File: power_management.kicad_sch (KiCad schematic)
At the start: 18 parts, among them Q1 Q_NMOS_DGS, Q2 Q_NMOS_DGS, U2 TLV803EA24DCKR

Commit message: WIP
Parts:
- added J2 (x3): Conn_01x04_Socket, Connector_PinHeader_2.54mm:PinHeader_1x04_P2.54mm_Vertical, symbol Connector:Conn_01x04_Socket
- R18: renamed from R17; footprint (none) -> Resistor_SMD:R_0603_1608Metric_Pad0.98x0.95mm_HandSolder
- R19: renamed from R18; footprint (none) -> Resistor_SMD:R_0603_1608Metric_Pad0.98x0.95mm_HandSolder
- R20: renamed from R19; footprint (none) -> Resistor_SMD:R_0603_1608Metric_Pad0.98x0.95mm_HandSolder
- R21: renamed from R20; footprint (none) -> Resistor_SMD:R_0603_1608Metric_Pad0.98x0.95mm_HandSolder
- R22: renamed from R21; footprint (none) -> Resistor_SMD:R_0603_1608Metric_Pad0.98x0.95mm_HandSolder
- R23: renamed from R22; footprint (none) -> Resistor_SMD:R_0603_1608Metric_Pad0.98x0.95mm_HandSolder
- R24: renamed from R23; footprint (none) -> Resistor_SMD:R_0603_1608Metric_Pad0.98x0.95mm_HandSolder
- R25: renamed from R24; footprint (none) -> Resistor_SMD:R_0603_1608Metric_Pad0.98x0.95mm_HandSolder
- R? (x2): footprint (none) -> Resistor_SMD:R_0603_1608Metric_Pad0.98x0.95mm_HandSolder
- U? (x2): footprint (none) -> Package_TO_SOT_SMD:SOT-23-6_Handsoldering
- renumbered R16 to R17
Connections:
- net EN_{PULSE}: now also J2.2 (Pin_2)
- net EN_{V_{BOOST3.3}}: now also J2.1 (Pin_1)
- net FORCE_ON: now also J2.2 (Pin_2)
- net GND: now also J2.1 (Pin_1)
- net SHD: now also J2.3 (Pin_3)
- net V_{ADP_SENSE_EN}: now also J2.1 (Pin_1)
- net V_{ADP_SENSE}: now also J2.2 (Pin_2)
- net V_{ADP}: now also J2.4 (Pin_4)
- net V_{RTC_SENSE_EN}: now also J2.3 (Pin_3)
- net V_{RTC_SENSE}: now also J2.4 (Pin_4)
- net V_{RTC}: now also J2.3 (Pin_3)
- no-connect marks 1 -> 2
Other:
- note added: "Open drain leakage current is max 350nA. The voltage drop across the pull-up resistor (V = IR): 0.00000035 amp * 1000000 ohm = 0.35V Typical is around 100nA: 0.0000001 amp * 1000000 ohm = 0.1V"

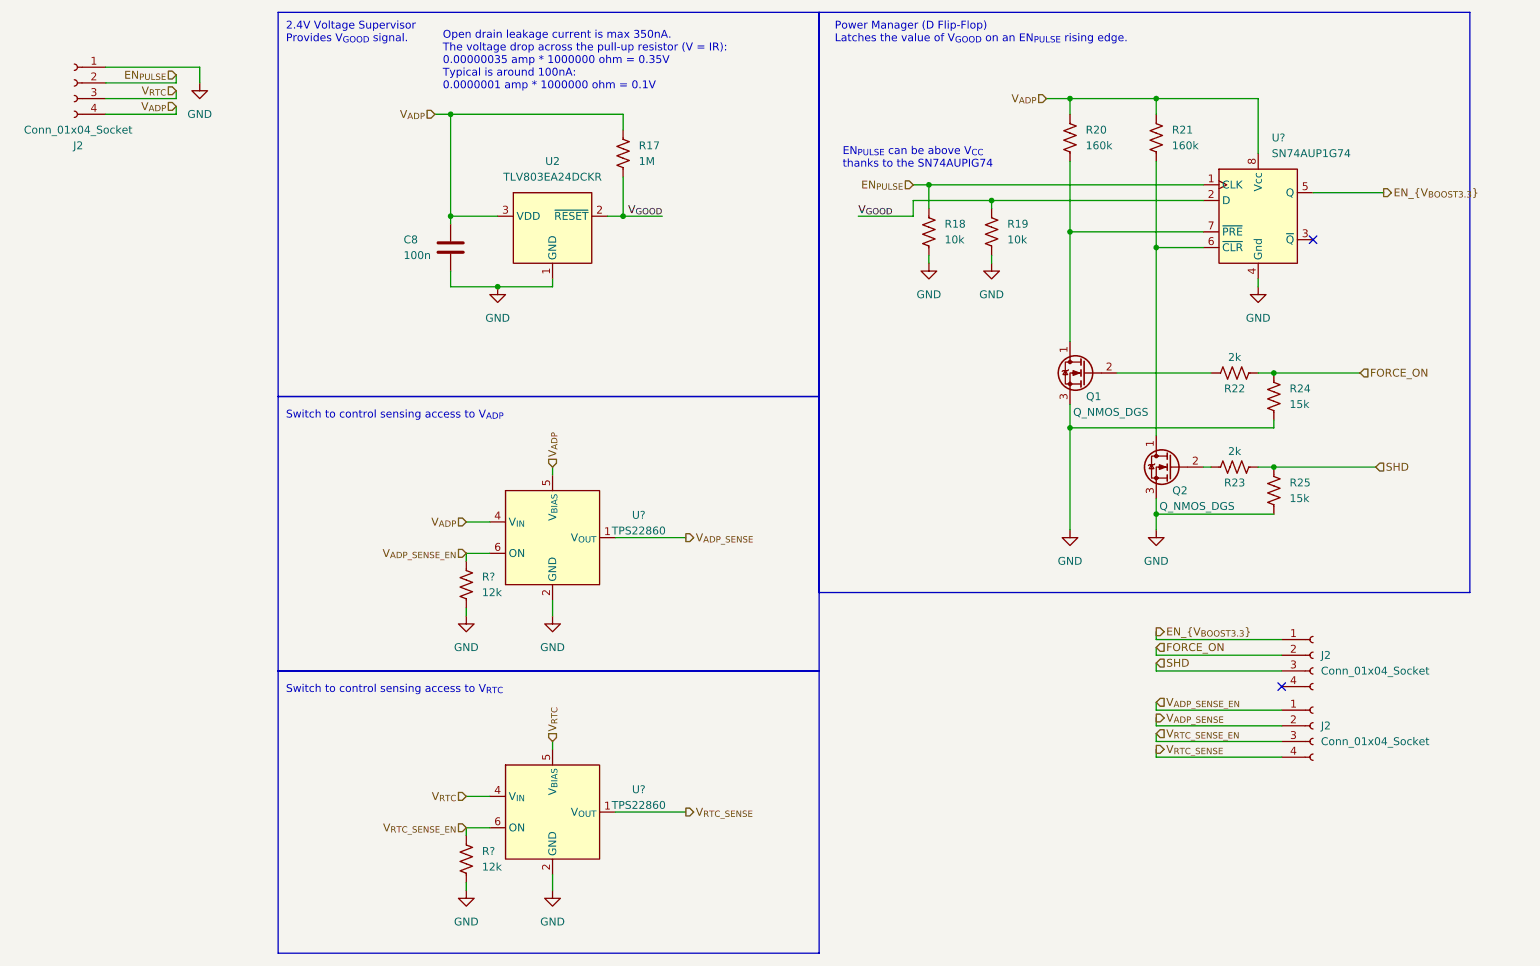
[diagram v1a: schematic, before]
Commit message: Layout cleanups, add more component data
 - Selected part for USB C socket
 - Tried to make more of the schematics compact and modular
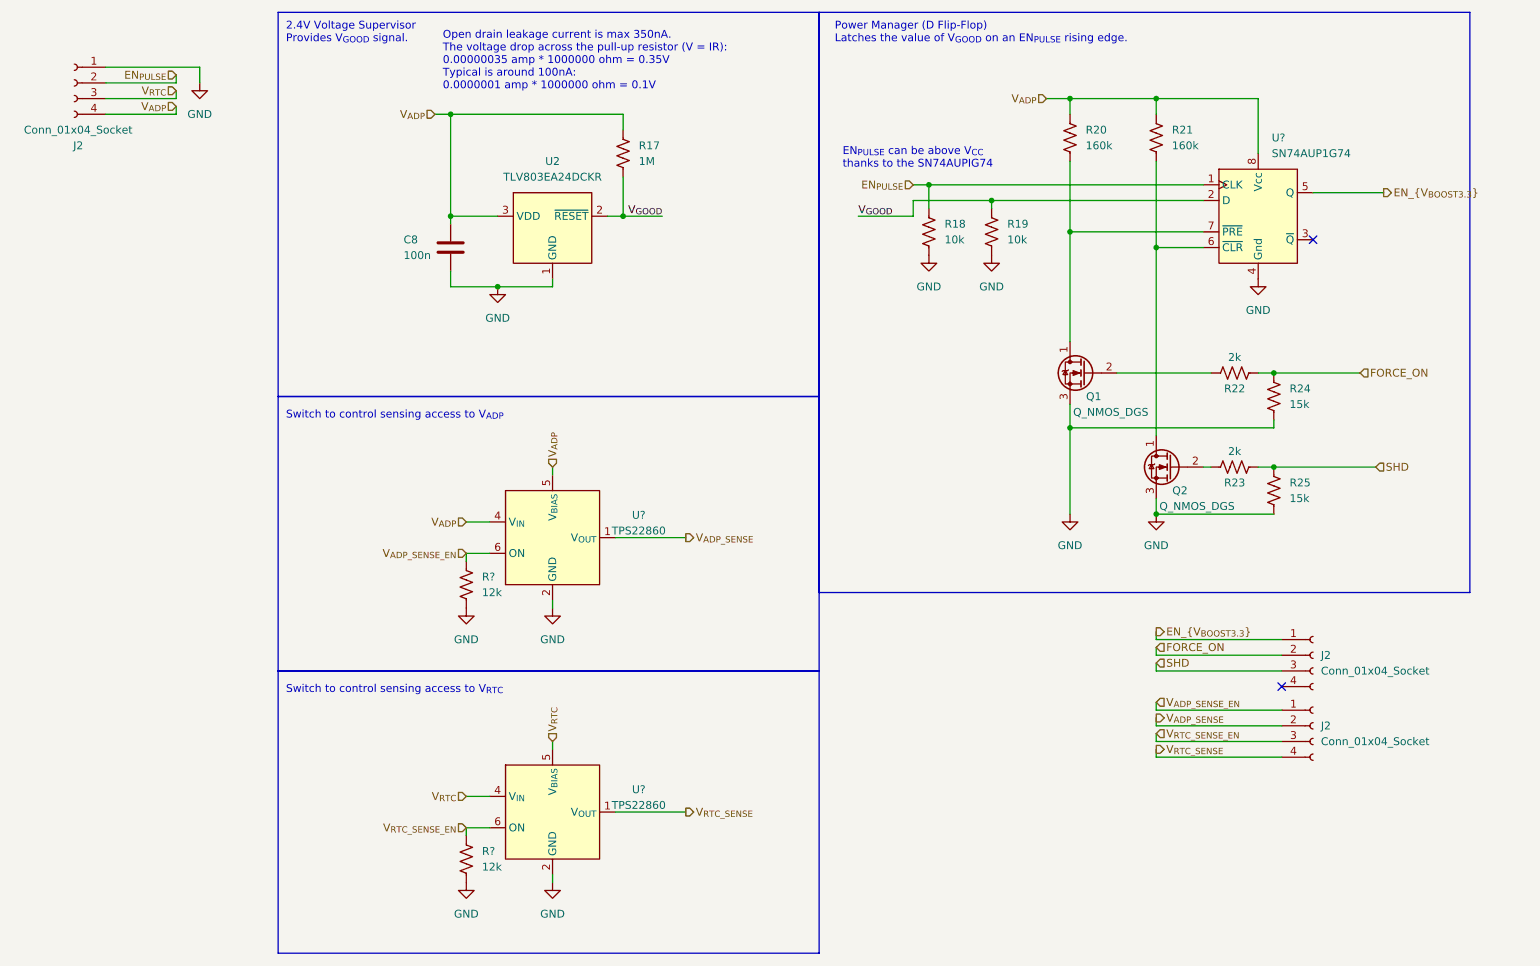
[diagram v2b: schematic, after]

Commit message: First routing attempt
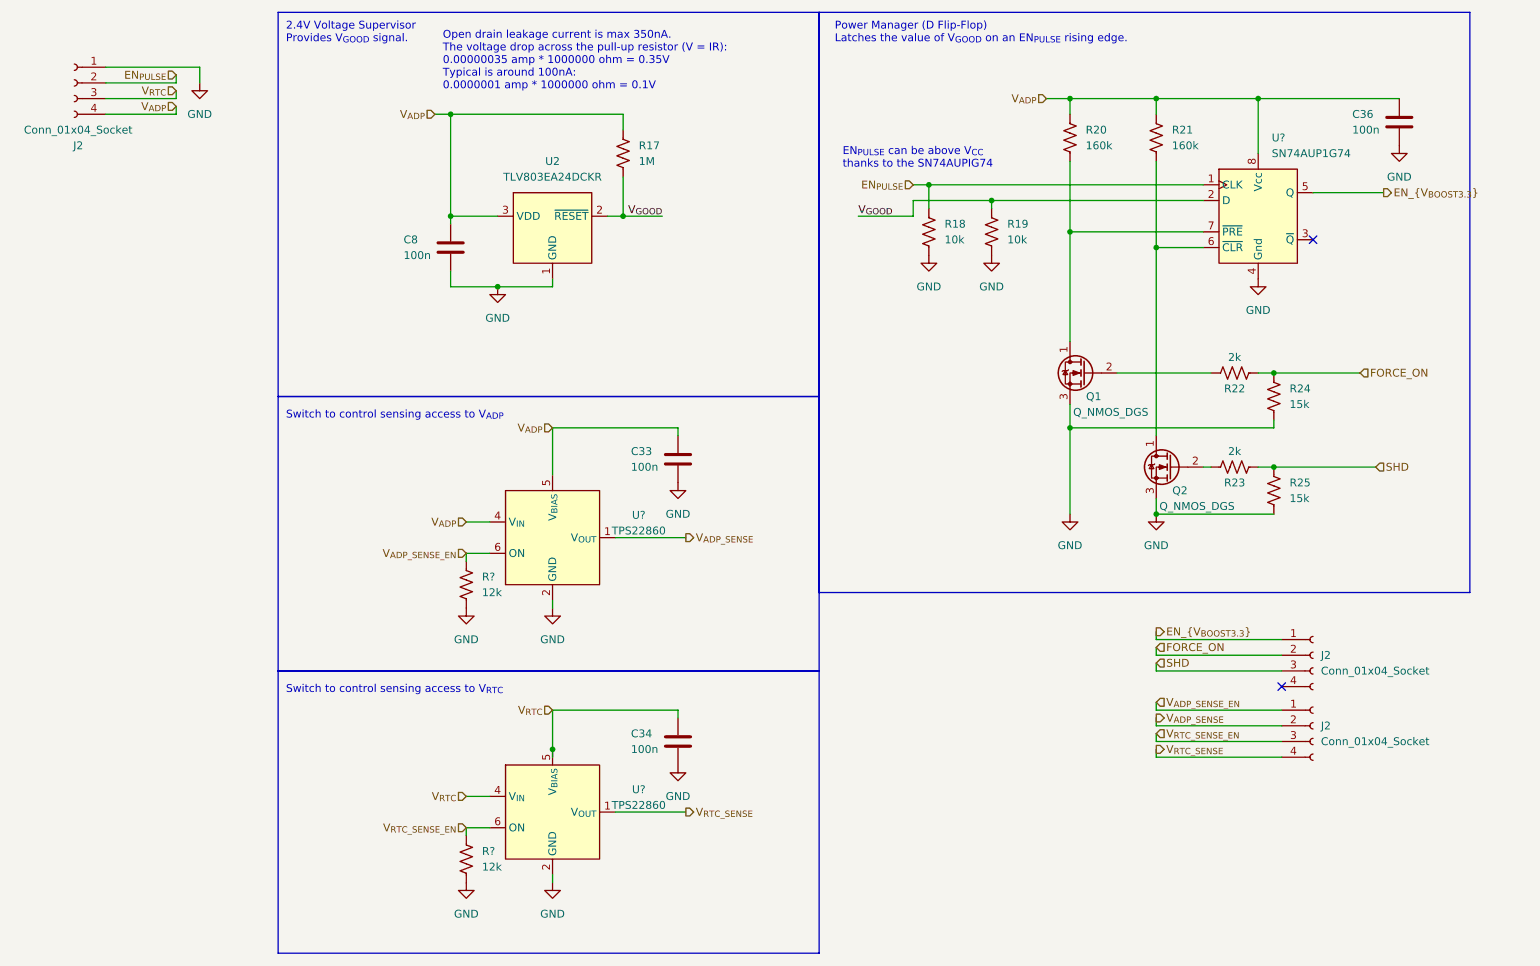
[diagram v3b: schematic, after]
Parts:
- added C33, C34, C36: 100n, Capacitor_SMD:C_0603_1608Metric_Pad1.08x0.95mm_HandSolder, symbol Device:C
- Q1, Q2: footprint (none) -> Package_TO_SOT_SMD:SOT-23_Handsoldering; Digikey Product Number (none) -> 4530-BSS123CT-ND
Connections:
- net GND: now also C33.2, C34.2, C36.2
- net V_{ADP}: now also C33.1, C36.1
- net V_{RTC}: now also C34.1

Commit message: Added LoRa module, lots of fixes & tweaks
 - Added loRa module as last Artemia experiment uses LoRa RFM95W
 - Added headers for debuggging purposes
 - Expanded board size to account for added hardware
 - Updated clearances to match JLCPCB manufacturing capabilities (I
   figure that if JLCPCB can fab it, anyone else can)
 - Fixed DRC issues (still need to run analysis on schematic)
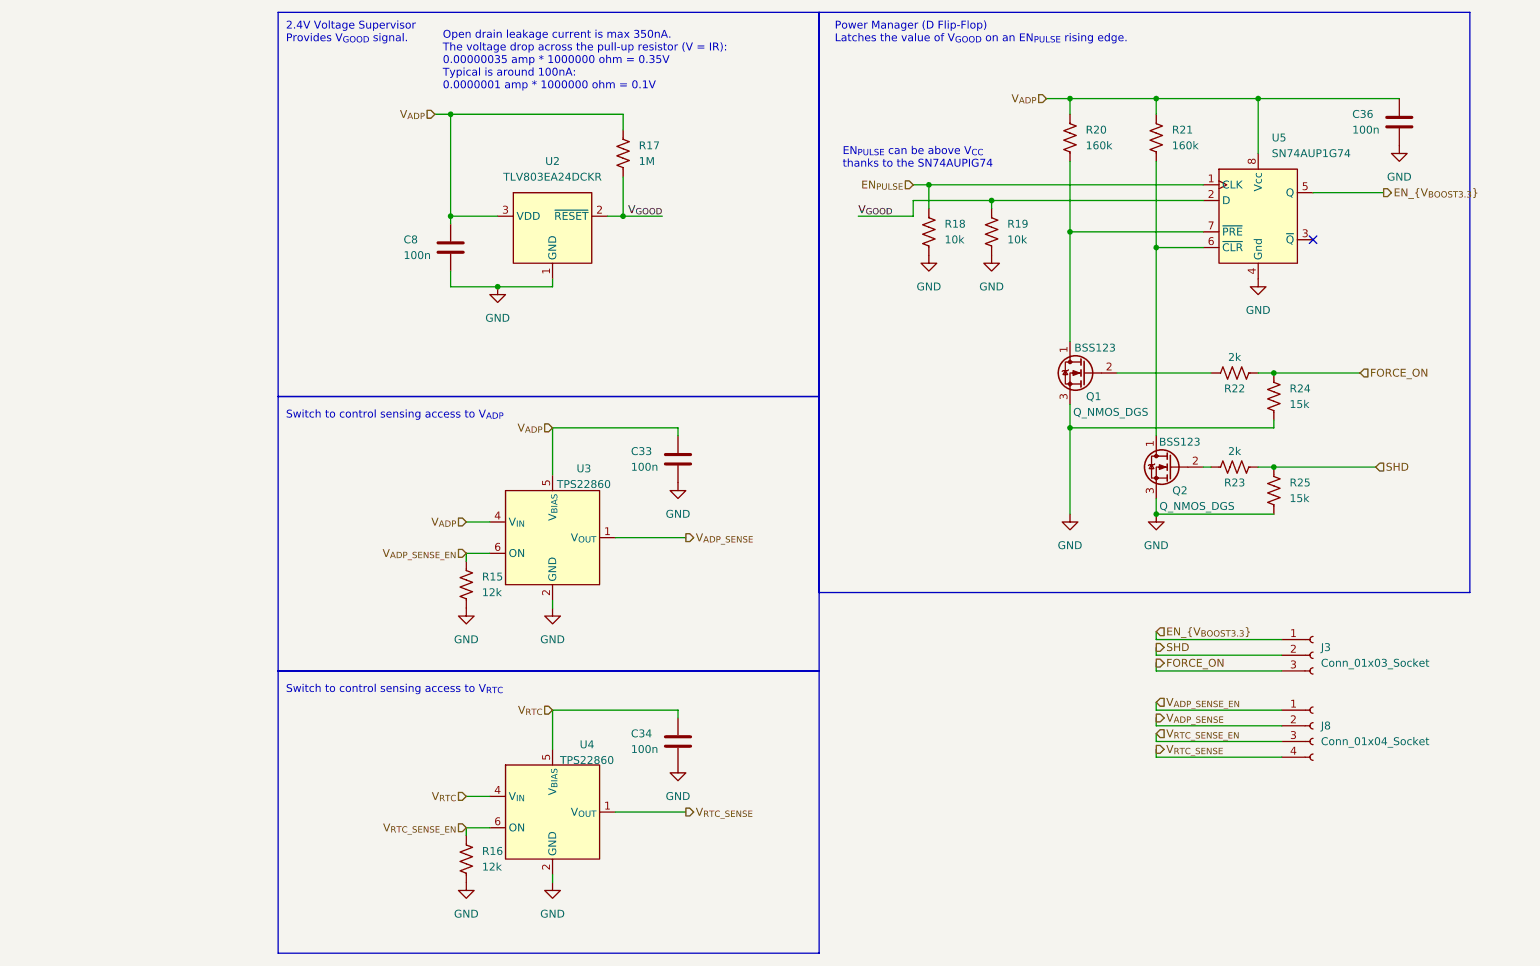
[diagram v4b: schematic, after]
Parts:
- removed J2 (x2): Conn_01x04_Socket, Connector_PinHeader_2.54mm:PinHeader_1x04_P2.54mm_Vertical, symbol Connector:Conn_01x04_Socket
- added J3: Conn_01x03_Socket, Connector_PinHeader_2.54mm:PinHeader_1x03_P2.54mm_Vertical, symbol Connector:Conn_01x03_Socket
- Q1, Q2: Manufacturer Product Number (none) -> BSS123
- U2: Digikey Product Number (none) -> 296-TLV803EA24DCKRTR-ND; Manufacturer Product Number (none) -> TLV803EA24DCKR
- U3, U4: renamed from U?; Digikey Product Number (none) -> 296-43982-2-ND; Manufacturer Product Number (none) -> TPS22860
- U5: renamed from U?; Digikey Product Number (none) -> 296-19761-2-ND; Manufacturer Product Number (none) -> SN74AUP1G74DCUR
- gave numbers to parts that had none: 2
- renumbered J2 to J8
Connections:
- net EN_{V_{BOOST3.3}}: now also J3.1 (Pin_1)
- net FORCE_ON: now also J3.3 (Pin_3)
- net SHD: now also J3.2 (Pin_2)
- no-connect marks 2 -> 1
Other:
- title: Artemia: Power Management -> Artemia: Power Management Subsystem
